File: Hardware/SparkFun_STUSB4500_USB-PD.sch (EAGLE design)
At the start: 49 parts, among them J4 QWIIC, Q1 9A/30V/15mΩ, U1 STUSB4500

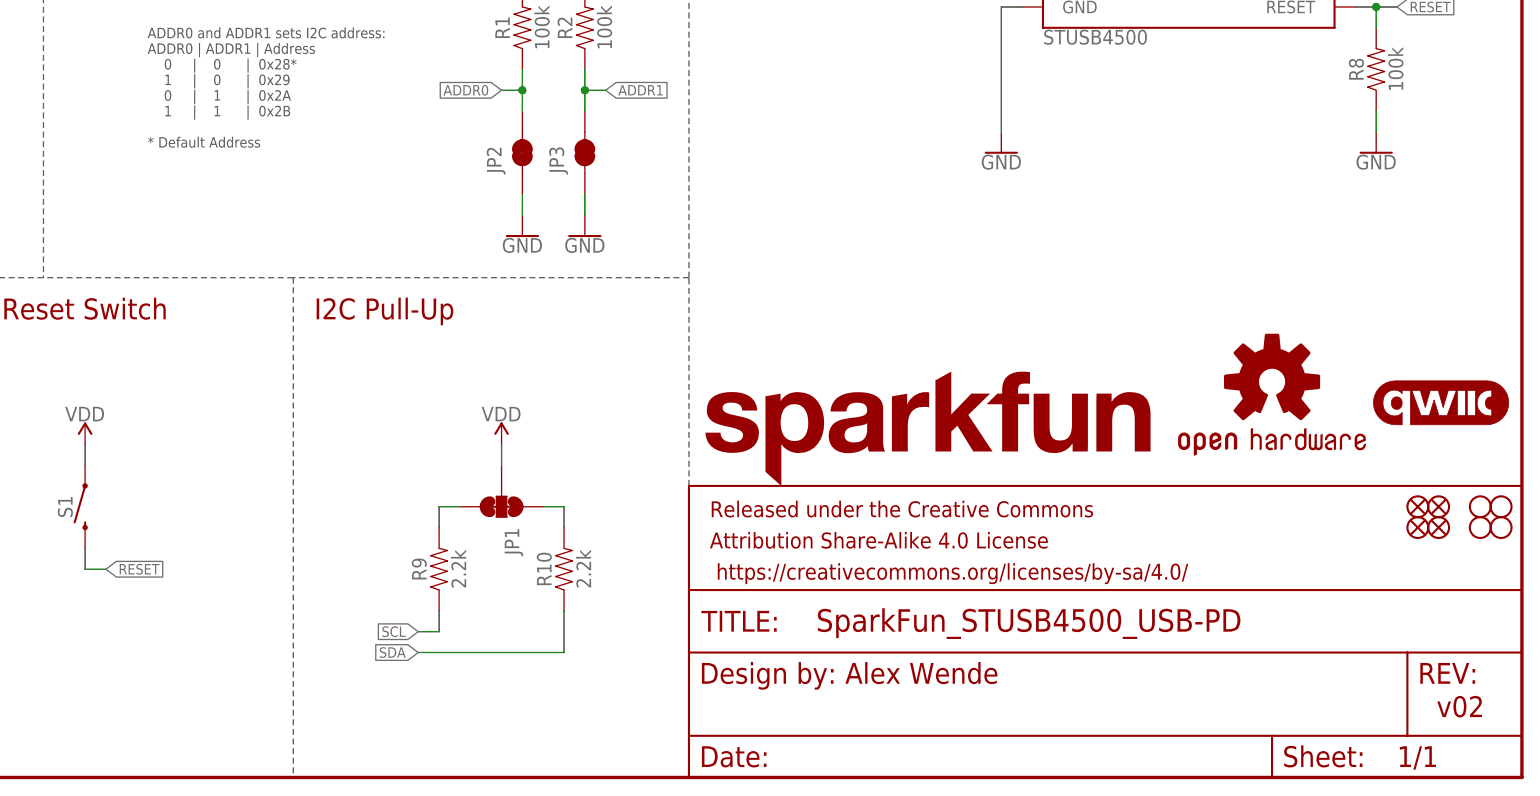
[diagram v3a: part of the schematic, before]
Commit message: v10 Update
- Updated STUSB4500 center pad paste
- Updated all text to vector
- Updated SCH to v10
- Added text about jumpers
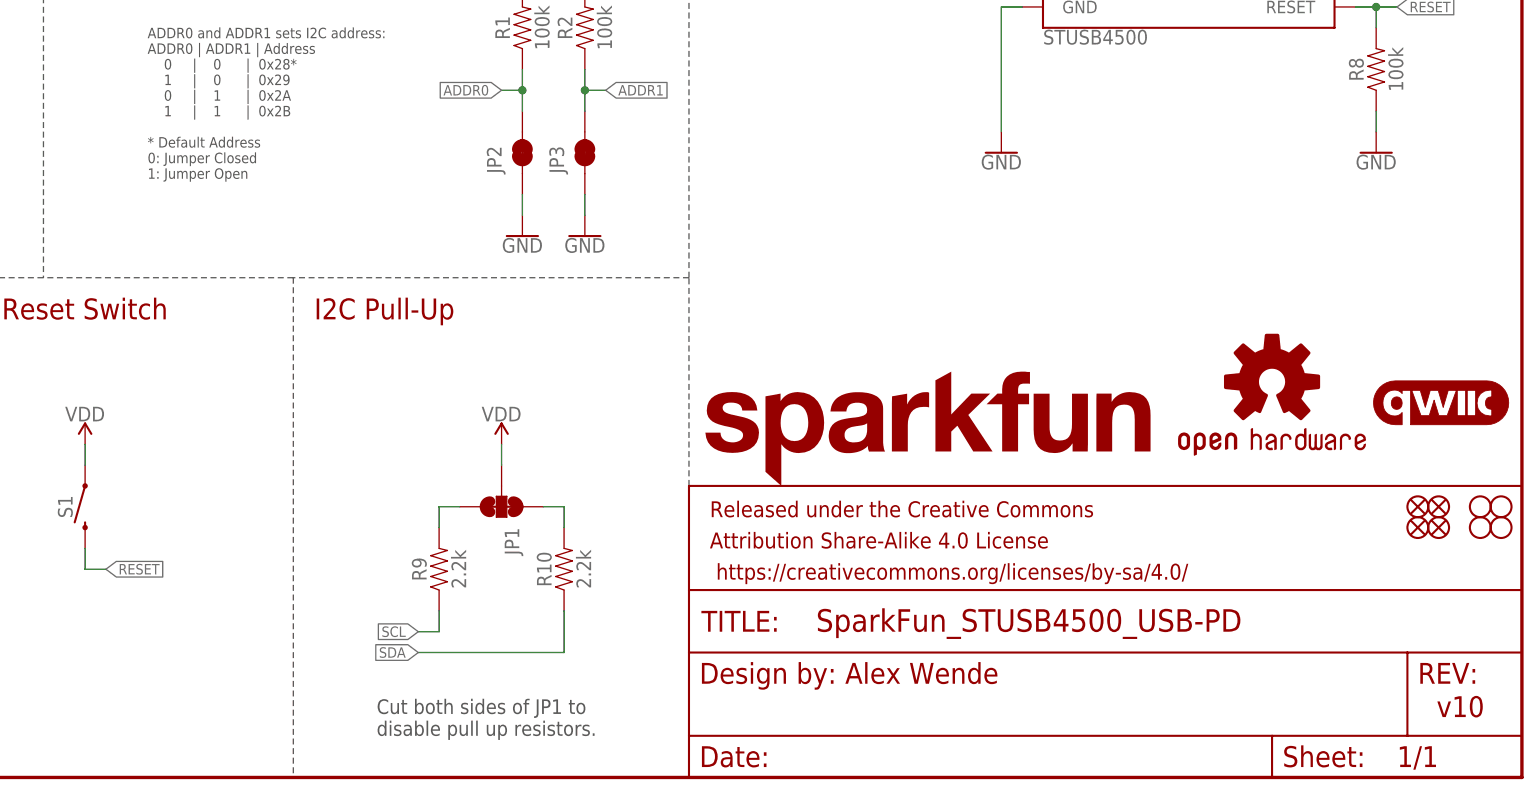
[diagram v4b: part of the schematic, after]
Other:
- note added: "ADDR0 and ADDR1 sets I2C address: ADDR0 | ADDR1 | Address 0 | 0 | 0x28* 1 | 0 | 0x29 0 | 1 | 0x2A 1 | 1 | 0x2B * Default Address 0: Jumper Closed 1: Jumper Open"
- note added: "Cut both sides of JP1 to disable pull up resistors."
- note added: "v10"
- note removed: "ADDR0 and ADDR1 sets I2C address: ADDR0 | ADDR1 | Address 0 | 0 | 0x28* 1 | 0 | 0x29 0 | 1 | 0x2A 1 | 1 | 0x2B * Default Address"
- note removed: "v02"
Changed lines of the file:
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@@
     0     |    1      |  0x2A
     1     |    1      |  0x2B
-* Default Address</text>
+* Default Address
+0: Jumper Closed
+1: Jumper Open</text>
 <text x="166.37" y="11.43" size="2.54" layer="94" font="vector">Alex Wende</text>
-<text x="238.506" y="7.366" size="2.54" layer="94" font="vector">v02</text>
+<text x="238.506" y="7.366" size="2.54" layer="94" font="vector">v10</text>
 <wire x1="147.32" y1="35.56" x2="147.32" y2="60.96" width="0.1524" layer="97" style="shortdash"/>
 <text x="149.86" y="180.34" size="2.54" layer="94" font="vector">STUSB4500</text>
@@
 <text x="200.66" y="170.18" size="1.778" layer="96" font="vector" rot="R90">7.6A/30V/
 29mΩ</text>
-<text x="2.54" y="104.14" size="2.54" layer="94">ESD Protection</text>
+<text x="2.54" y="104.14" size="2.54" layer="94" font="vector">ESD Protection</text>
 <text x="7.62" y="132.08" size="2.54" layer="97" font="vector">VDD (optional): 3.0 - 5.5V</text>
+<text x="109.22" y="5.08" size="1.778" layer="97" font="vector">Cut both sides of JP1 to
+disable pull up resistors.</text>
 </plain>
 <instances>
@@
 </instance>
 <instance part="SUPPLY3" gate="G$1" x="45.72" y="93.98" smashed="yes">
-<attribute name="VALUE" x="45.72" y="96.774" size="1.778" layer="96" align="bottom-center"/>
+<attribute name="VALUE" x="45.72" y="96.774" size="1.778" layer="96" font="vector" align="bottom-center"/>
 </instance>
 <instance part="SUPPLY13" gate="G$1" x="15.24" y="93.98" smashed="yes">
-<attribute name="VALUE" x="15.24" y="96.774" size="1.778" layer="96" align="bottom-center"/>
+<attribute name="VALUE" x="15.24" y="96.774" size="1.778" layer="96" font="vector" align="bottom-center"/>
 </instance>
 <instance part="GND14" gate="1" x="45.72" y="76.2" smashed="yes">
-<attribute name="VALUE" x="45.72" y="75.946" size="1.778" layer="96" align="top-center"/>
+<attribute name="VALUE" x="45.72" y="75.946" size="1.778" layer="96" font="vector" align="top-center"/>
 </instance>
 <instance part="GND15" gate="1" x="35.56" y="76.2" smashed="yes">
-<attribute name="VALUE" x="35.56" y="75.946" size="1.778" layer="96" align="top-center"/>
+<attribute name="VALUE" x="35.56" y="75.946" size="1.778" layer="96" font="vector" align="top-center"/>
 </instance>
 <instance part="GND20" gate="1" x="25.4" y="76.2" smashed="yes">
-<attribute name="VALUE" x="25.4" y="75.946" size="1.778" layer="96" align="top-center"/>
+<attribute name="VALUE" x="25.4" y="75.946" size="1.778" layer="96" font="vector" align="top-center"/>
 </instance>
 <instance part="GND21" gate="1" x="15.24" y="76.2" smashed="yes">
-<attribute name="VALUE" x="15.24" y="75.946" size="1.778" layer="96" align="top-center"/>
+<attribute name="VALUE" x="15.24" y="75.946" size="1.778" layer="96" font="vector" align="top-center"/>
 </instance>
 <instance part="D4" gate="G$1" x="160.02" y="127" smashed="yes" rot="R90">
@@
 </instance>
 <instance part="SUPPLY5" gate="VDD" x="160.02" y="132.08" smashed="yes">
-<attribute name="VALUE" x="160.02" y="134.874" size="1.778" layer="96" align="bottom-center"/>
+<attribute name="VALUE" x="160.02" y="134.874" size="1.778" layer="96" font="vector" align="bottom-center"/>
 </instance>
 <instance part="SUPPLY6" gate="VDD" x="111.76" y="170.18" smashed="yes">
-<attribute name="VALUE" x="111.76" y="172.974" size="1.778" layer="96" align="bottom-center"/>
+<attribute name="VALUE" x="111.76" y="172.974" size="1.778" layer="96" font="vector" align="bottom-center"/>
 </instance>
 <instance part="SUPPLY7" gate="VDD" x="78.74" y="139.7" smashed="yes">
-<attribute name="VALUE" x="78.74" y="142.494" size="1.778" layer="96" align="bottom-center"/>
+<attribute name="VALUE" x="78.74" y="142.494" size="1.778" layer="96" font="vector" align="bottom-center"/>
 </instance>
 <instance part="SUPPLY8" gate="VDD" x="17.78" y="45.72" smashed="yes">
-<attribute name="VALUE" x="17.78" y="48.514" size="1.778" layer="96" align="bottom-center"/>
+<attribute name="VALUE" x="17.78" y="48.514" size="1.778" layer="96" font="vector" align="bottom-center"/>
 </instance>
 <instance part="SUPPLY9" gate="VDD" x="30.48" y="45.72" smashed="yes">
-<attribute name="VALUE" x="30.48" y="48.514" size="1.778" layer="96" align="bottom-center"/>
+<attribute name="VALUE" x="30.48" y="48.514" size="1.778" layer="96" font="vector" align="bottom-center"/>
 </instance>
 <instance part="SUPPLY11" gate="VDD" x="43.18" y="45.72" smashed="yes">
-<attribute name="VALUE" x="43.18" y="48.514" size="1.778" layer="96" align="bottom-center"/>
+<attribute name="VALUE" x="43.18" y="48.514" size="1.778" layer="96" font="vector" align="bottom-center"/>
 </instance>
 <instance part="SUPPLY12" gate="VDD" x="73.66" y="40.64" smashed="yes">
-<attribute name="VALUE" x="73.66" y="43.434" size="1.778" layer="96" align="bottom-center"/>
+<attribute name="VALUE" x="73.66" y="43.434" size="1.778" layer="96" font="vector" align="bottom-center"/>
 </instance>
 <instance part="SUPPLY14" gate="VDD" x="124.46" y="40.64" smashed="yes">
-<attribute name="VALUE" x="124.46" y="43.434" size="1.778" layer="96" align="bottom-center"/>
+<attribute name="VALUE" x="124.46" y="43.434" size="1.778" layer="96" font="vector" align="bottom-center"/>
 </instance>
 <instance part="SUPPLY16" gate="VDD" x="127" y="99.06" smashed="yes">
-<attribute name="VALUE" x="127" y="101.854" size="1.778" layer="96" align="bottom-center"/>
+<attribute name="VALUE" x="127" y="101.854" size="1.778" layer="96" font="vector" align="bottom-center"/>
 </instance>
 <instance part="SUPPLY19" gate="VDD" x="134.62" y="99.06" smashed="yes">
-<attribute name="VALUE" x="134.62" y="101.854" size="1.778" layer="96" align="bottom-center"/>
+<attribute name="VALUE" x="134.62" y="101.854" size="1.778" layer="96" font="vector" align="bottom-center"/>
 </instance>
 <instance part="SUPPLY1" gate="VDD" x="185.42" y="139.7" smashed="yes">
-<attribute name="VALUE" x="185.42" y="142.494" size="1.778" layer="96" align="bottom-center"/>
+<attribute name="VALUE" x="185.42" y="142.494" size="1.778" layer="96" font="vector" align="bottom-center"/>
 </instance>
 <instance part="J7" gate="J1" x="78.74" y="162.56" smashed="yes" rot="MR180">
@@
 <pinref part="D6" gate="G$1" pin="C"/>
 <wire x1="25.4" y1="91.44" x2="25.4" y2="93.98" width="0.1524" layer="91"/>
-<label x="25.4" y="93.98" size="1.27" layer="95" rot="R90" xref="yes"/>
+<label x="25.4" y="93.98" size="1.27" layer="95" font="vector" rot="R90" xref="yes"/>
 </segment>
 </net>
@@
 <pinref part="D7" gate="G$1" pin="C"/>
 <wire x1="35.56" y1="91.44" x2="35.56" y2="93.98" width="0.1524" layer="91"/>
-<label x="35.56" y="93.98" size="1.27" layer="95" rot="R90" xref="yes"/>
+<label x="35.56" y="93.98" size="1.27" layer="95" font="vector" rot="R90" xref="yes"/>
 </segment>
 </net>
@@
 <pinref part="U1" gate="G$1" pin="GPIO"/>
 <wire x1="228.6" y1="121.92" x2="231.14" y2="121.92" width="0.1524" layer="91"/>
-<label x="231.14" y="121.92" size="1.27" layer="95" xref="yes"/>
+<label x="231.14" y="121.92" size="1.27" layer="95" font="vector" xref="yes"/>
 </segment>
 <segment>
 <pinref part="D1" gate="G$1" pin="C"/>
 <wire x1="17.78" y1="22.86" x2="17.78" y2="20.32" width="0.1524" layer="91"/>
-<label x="17.78" y="20.32" size="1.27" layer="95" rot="R270" xref="yes"/>
+<label x="17.78" y="20.32" size="1.27" layer="95" font="vector" rot="R270" xref="yes"/>
 </segment>
 <segment>
 <pinref part="J7" gate="J1" pin="7"/>
 <wire x1="83.82" y1="152.4" x2="88.9" y2="152.4" width="0.1524" layer="91"/>
-<label x="88.9" y="152.4" size="1.27" layer="95" xref="yes"/>
-</segment>
-</net>
+<label x="88.9" y="152.4" size="1.27" layer="95" font="vector" xref="yes"/>
+</segment>
+</net>

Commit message: v10
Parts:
- Q1: device stusb4500:MOSFET_PCH-STL9P3LLH6 -> SparkFun-DiscreteSemi:MOSFET_PCH-STL9P3LLH6
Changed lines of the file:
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@@
 <part name="R7" library="SparkFun-Resistors" deviceset="1KOHM" device="-0603-1/10W-1%" value="1k"/>
 <part name="C3" library="SparkFun-Capacitors" deviceset="0.1UF" device="-0603-100V-10%" value="0.1uF"/>
-<part name="Q1" library="stusb4500" deviceset="MOSFET_PCH" device="-STL9P3LLH6" value="9A/30V/15mΩ"/>
+<part name="Q1" library="SparkFun-DiscreteSemi" deviceset="MOSFET_PCH" device="-STL9P3LLH6" value="9A/30V/15mΩ"/>
 <part name="R8" library="SparkFun-Resistors" deviceset="100KOHM" device="-0603-1/10W-1%" value="100k"/>
 <part name="GND7" library="SparkFun-PowerSymbols" deviceset="GND" device=""/>
